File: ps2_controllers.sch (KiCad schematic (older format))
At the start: 11 parts

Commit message: Passing ERC
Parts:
- gave numbers to parts that had none: 11
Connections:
- wire segments 45 -> 49
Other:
- moved on the sheet: D8, D9, P3, P4, R25, R26, R27, R28, R29, R30, SW1

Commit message: Starting on netlist
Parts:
- R25: footprint (none) -> Resistors_SMD:R_0603
- R26, R27, R30: footprint Resistors_SMD:R_0805_HandSoldering -> Resistors_SMD:R_0603
- R28, R29: footprint Resistors_SMD:R_0805_HandSoldering -> Resistors_SMD:R_0805
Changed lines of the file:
@@
 LIBS:w_device
 LIBS:pcb_ledtorus_controller-cache
-LIBS:tiva_pcb1-cache
 EELAYER 26 0
 EELAYER END
@@
 F 0 "R28" V 4130 1800 50  0000 C CNN
 F 1 "1k" V 4050 1800 50  0000 C CNN
-F 2 "Resistors_SMD:R_0805_HandSoldering" V 3980 1800 30  0001 C CNN
+F 2 "Resistors_SMD:R_0805" V 3980 1800 30  0001 C CNN
 F 3 "" H 4050 1800 30  0000 C CNN
 	1    4050 1800
@@
 F 0 "R29" V 5030 1800 50  0000 C CNN
 F 1 "1k" V 4950 1800 50  0000 C CNN
-F 2 "Resistors_SMD:R_0805_HandSoldering" V 4880 1800 30  0001 C CNN
+F 2 "Resistors_SMD:R_0805" V 4880 1800 30  0001 C CNN
 F 3 "" H 4950 1800 30  0000 C CNN
 	1    4950 1800
@@
 F 0 "R26" V 2130 1750 50  0000 C CNN
 F 1 "4k7" V 2050 1750 50  0000 C CNN
-F 2 "Resistors_SMD:R_0805_HandSoldering" V 1980 1750 30  0001 C CNN
+F 2 "Resistors_SMD:R_0603" V 1980 1750 30  0001 C CNN
 F 3 "" H 2050 1750 30  0000 C CNN
 	1    2050 1750
@@
 F 0 "R30" V 2130 3650 50  0000 C CNN
 F 1 "4k7" V 2050 3650 50  0000 C CNN
-F 2 "Resistors_SMD:R_0805_HandSoldering" V 1980 3650 30  0001 C CNN
+F 2 "Resistors_SMD:R_0603" V 1980 3650 30  0001 C CNN
 F 3 "" H 2050 3650 30  0000 C CNN
 	1    2050 3650
@@
 F 0 "R27" V 2780 1750 50  0000 C CNN
 F 1 "4k7" V 2700 1750 50  0000 C CNN
-F 2 "Resistors_SMD:R_0805_HandSoldering" V 2630 1750 30  0001 C CNN
+F 2 "Resistors_SMD:R_0603" V 2630 1750 30  0001 C CNN
 F 3 "" H 2700 1750 30  0000 C CNN
 	1    2700 1750
@@
 F 0 "R25" V 1750 1500 50  0000 C CNN
 F 1 "4k7" V 1850 1500 40  0000 C CNN
-F 2 "" H 1850 1500 50  0001 C CNN
+F 2 "Resistors_SMD:R_0603" H 1850 1500 50  0001 C CNN
 F 3 "" H 1850 1500 50  0001 C CNN
 	1    1850 1500

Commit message: Work on layout
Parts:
- removed D8, D9: LED, LEDs:LED_0805, symbol LED
- removed R28, R29: 1k, Resistors_SMD:R_0805, symbol R
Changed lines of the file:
@@
 	1    0    0    -1
-$EndComp
-$Comp
-L LED D8
-U 1 1 5C262DAB
-P 4050 1550
-F 0 "D8" H 4050 1650 50  0000 C CNN
-F 1 "LED" H 4050 1450 50  0000 C CNN
-F 2 "LEDs:LED_0805" H 4050 1550 60  0001 C CNN
-F 3 "" H 4050 1550 60  0000 C CNN
-	1    4050 1550
-	-1   0    0    -1
-$EndComp
-$Comp
-L LED D9
-U 1 1 5C262DAC
-P 4950 1550
-F 0 "D9" H 4950 1650 50  0000 C CNN
-F 1 "LED" H 4950 1450 50  0000 C CNN
-F 2 "LEDs:LED_0805" H 4950 1550 60  0001 C CNN
-F 3 "" H 4950 1550 60  0000 C CNN
-	1    4950 1550
-	-1   0    0    -1
 $EndComp
 Text Notes 1000 1325 0    120  ~ 24
@@
 Text Notes 1000 3350 0    120  ~ 24
 DualShock2, 2
-$Comp
-L R R28
-U 1 1 5C262DAD
-P 4050 1800
-F 0 "R28" V 4130 1800 50  0000 C CNN
-F 1 "1k" V 4050 1800 50  0000 C CNN
-F 2 "Resistors_SMD:R_0805" V 3980 1800 30  0001 C CNN
-F 3 "" H 4050 1800 30  0000 C CNN
-	1    4050 1800
-	0    1    1    0
-$EndComp
-$Comp
-L R R29
-U 1 1 5C262DAE
-P 4950 1800
-F 0 "R29" V 5030 1800 50  0000 C CNN
-F 1 "1k" V 4950 1800 50  0000 C CNN
-F 2 "Resistors_SMD:R_0805" V 4880 1800 30  0001 C CNN
-F 3 "" H 4950 1800 30  0000 C CNN
-	1    4950 1800
-	0    1    1    0
-$EndComp
 $Comp
 L R R26
@@
 	-1   0    0    1
 $EndComp
-Text Label 4225 1550 0    60   ~ 0
-gpio1
-Text Label 5125 1550 0    60   ~ 0
-gpio2
 Text Label 5775 1950 0    60   ~ 0
 gpio1
@@
 	1    0    0    -1
 $EndComp
-$Comp
-L +3V3 #PWR031
-U 1 1 5C262DB5
-P 5375 1850
-F 0 "#PWR031" H 5375 1700 50  0001 C CNN
-F 1 "+3V3" H 5393 2023 50  0000 C CNN
-F 2 "" H 5375 1850 50  0000 C CNN
-F 3 "" H 5375 1850 50  0000 C CNN
-	1    5375 1850
-	1    0    0    -1
-$EndComp
 Wire Wire Line
 	1500 1600 1700 1600
@@
 Wire Wire Line
 	1600 4000 1600 4475
-Wire Wire Line
-	3900 1550 3900 1800
-Wire Wire Line
-	4800 1550 4800 1800
-Wire Wire Line
-	4200 1800 4300 1800
-Wire Wire Line
-	4300 1800 4300 1950
-Wire Wire Line
-	5100 1800 5175 1800
-Wire Wire Line
-	5175 1800 5175 1950
-Wire Wire Line
-	4200 1550 4500 1550
-Wire Wire Line
-	5100 1550 6050 1550
 Wire Wire Line
 	5750 1950 6050 1950
@@
 	6650 1750 7000 1750
 Connection ~ 7000 1750
-Wire Wire Line
-	4300 1950 5375 1950
-Wire Wire Line
-	5375 1950 5375 1850
-Connection ~ 5175 1950
 Text GLabel 1600 1800 2    45   Input ~ 0
 ps2_clk
@@
 Connection ~ 5600 1550
 Wire Wire Line
-	4500 1550 4500 2050
-Wire Wire Line
-	4500 2050 5750 2050
-Wire Wire Line
 	5750 2050 5750 1950
 Text GLabel 5600 1950 1    45   Output ~ 0
@@
 	5600 1950 5600 2050
 Connection ~ 5600 2050
+Wire Wire Line
+	5600 1550 6050 1550
+Wire Wire Line
+	5600 2050 5750 2050
 $EndSCHEMATC

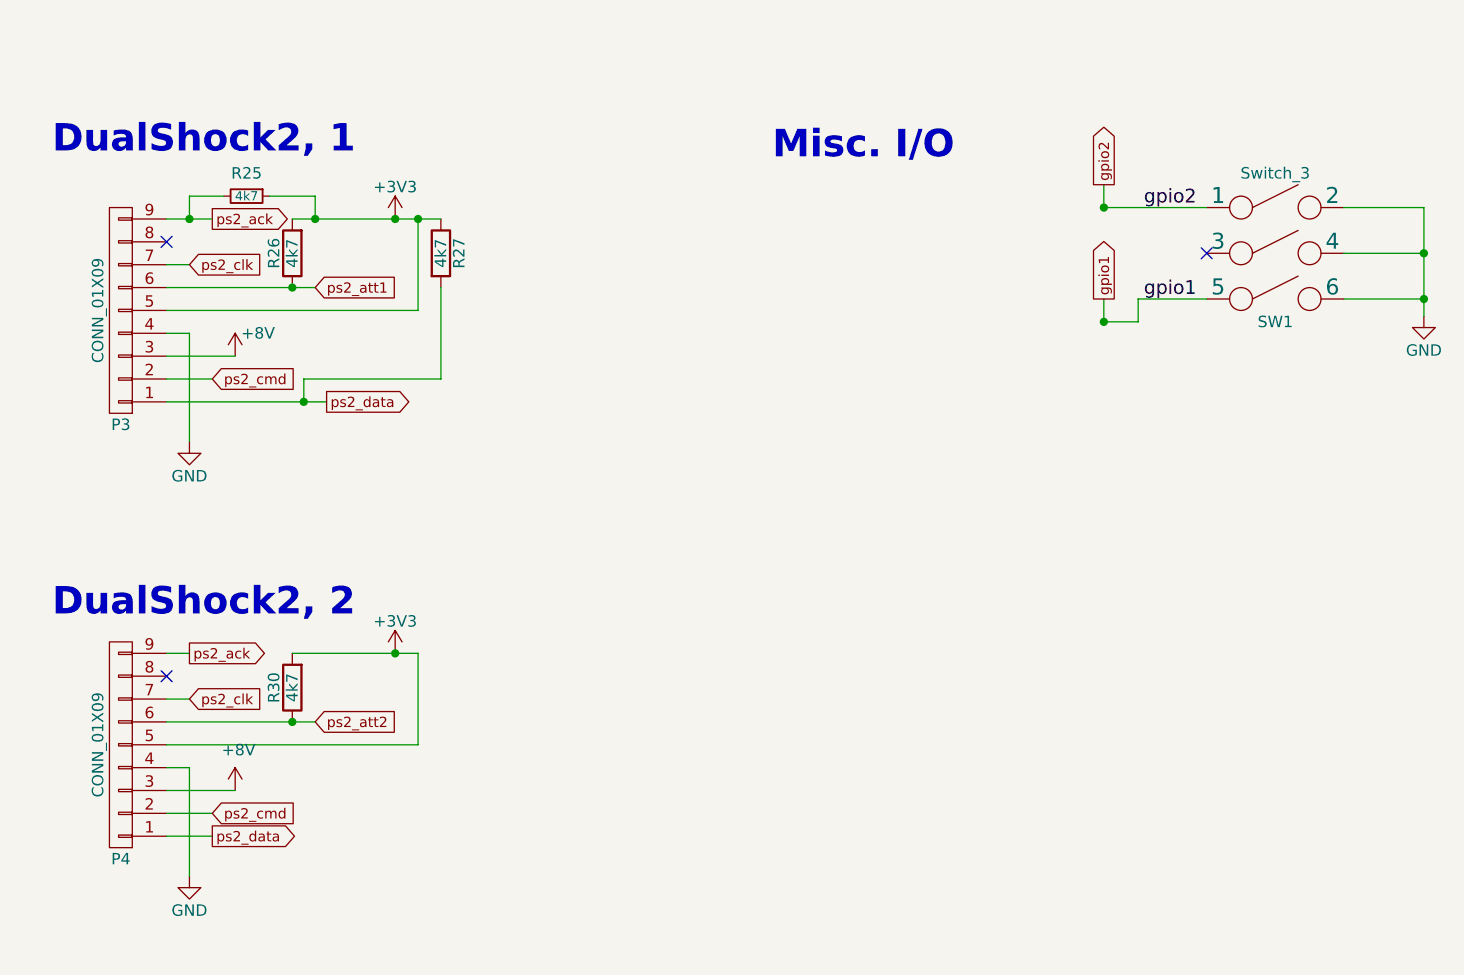
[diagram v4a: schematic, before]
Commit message: Completing cleanups and ToDos:
 - L6234 thermal vias done
 - Gerbers checked
 - Misc. io and stuff tweaks
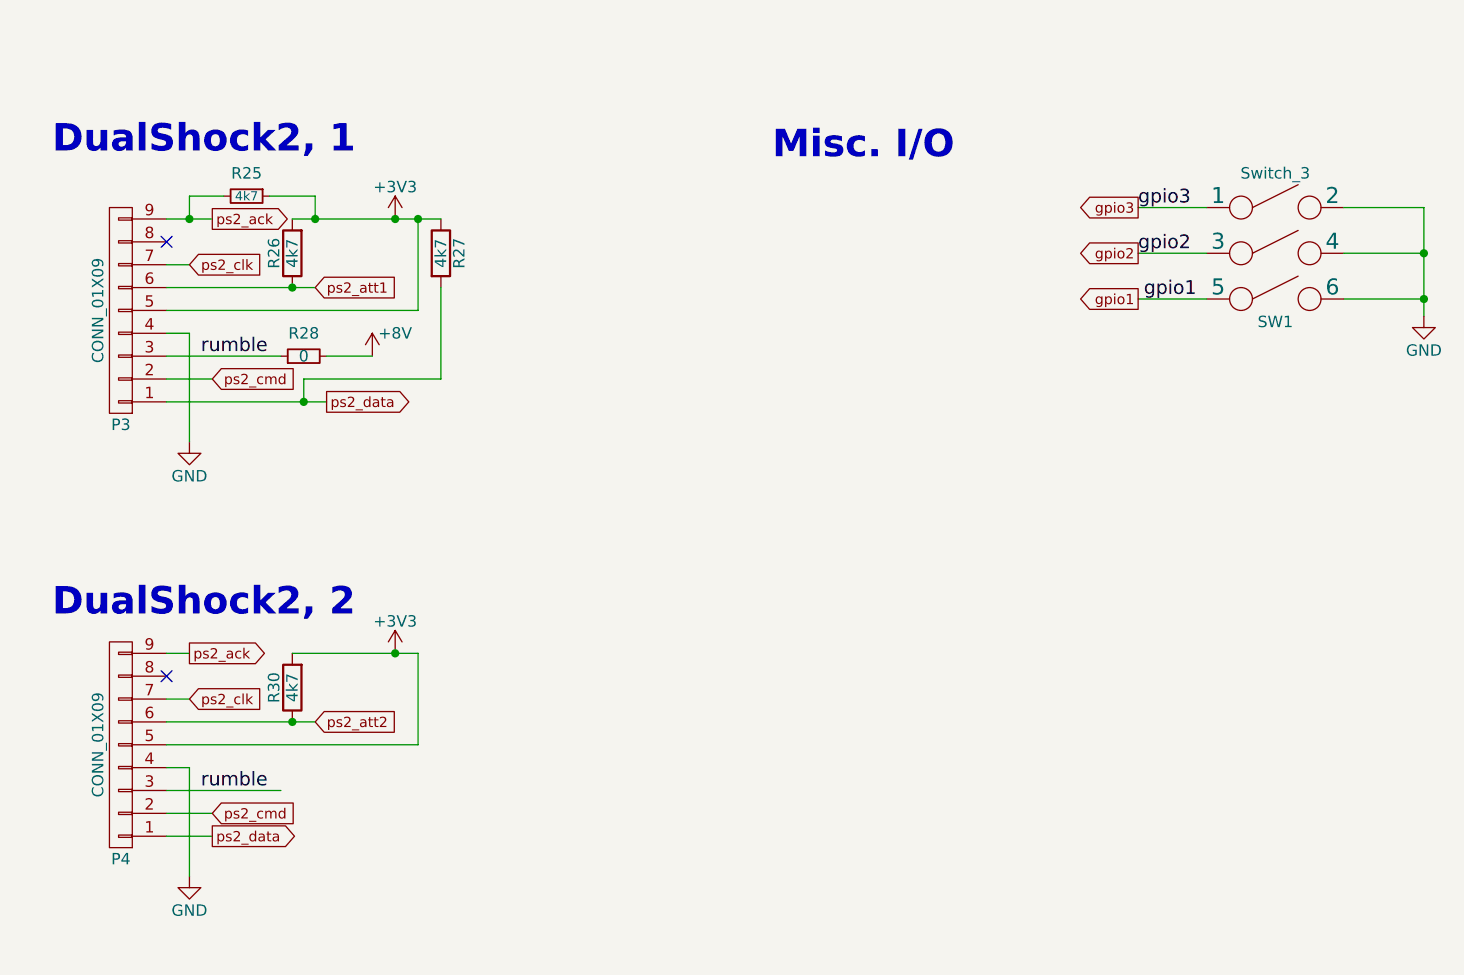
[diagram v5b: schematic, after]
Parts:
- added R28: 0, Resistors_SMD:R_0805, symbol R_Small
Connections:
- net +8V: now also R28.2; no longer P3.3 (P3), P4.3 (P3)
- net gpio2: now also SW1.3; no longer SW1.1
- new net gpio3: SW1.1
- new net rumble: P3.3 (P3), P4.3 (P3), R28.1
- no-connect marks 3 -> 2
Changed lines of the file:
@@
 Text Label 5775 1950 0    60   ~ 0
 gpio1
-Text Label 5775 1550 0    60   ~ 0
+Text Label 5750 1750 0    60   ~ 0
 gpio2
 $Comp
@@
 	1    0    0    -1
 $EndComp
-NoConn ~ 6050 1750
 $Comp
 L R R27
@@
 	1500 2100 1600 2100
 Wire Wire Line
-	1500 2200 1800 2200
+	1500 2200 2000 2200
 Wire Wire Line
 	1500 2300 1700 2300
@@
 	1500 3800 2150 3800
 Wire Wire Line
-	1500 4100 1800 4100
+	1500 4100 2000 4100
 Wire Wire Line
 	1600 2100 1600 2575
@@
 L +8V #PWR033
 U 1 1 5C2803CB
-P 1800 2200
-F 0 "#PWR033" H 1800 2050 50  0001 C CNN
-F 1 "+8V" H 1900 2300 50  0000 C CNN
-F 2 "" H 1800 2200 50  0001 C CNN
-F 3 "" H 1800 2200 50  0001 C CNN
-	1    1800 2200
+P 2400 2200
+F 0 "#PWR033" H 2400 2050 50  0001 C CNN
+F 1 "+8V" H 2500 2300 50  0000 C CNN
+F 2 "" H 2400 2200 50  0001 C CNN
+F 3 "" H 2400 2200 50  0001 C CNN
+	1    2400 2200
 	1    0    0    -1
 $EndComp
 Connection ~ 2100 2400
 Wire Wire Line
-	2600 2000 2600 1600
+	2600 1600 2600 2000
 Wire Wire Line
 	2050 1600 2700 1600
@@
 	1500 3900 2600 3900
 Wire Wire Line
-	2600 3900 2600 3500
+	2600 3500 2600 3900
 Wire Wire Line
-	2600 3500 2050 3500
+	2050 3500 2600 3500
 Connection ~ 2500 3500
 Text GLabel 2150 3800 2    45   Input ~ 0
 ps2_att2
 Connection ~ 2050 3800
-$Comp
-L +8V #PWR036
-U 1 1 5C281018
-P 1800 4100
-F 0 "#PWR036" H 1800 3950 50  0001 C CNN
-F 1 "+8V" H 1815 4277 50  0000 C CNN
-F 2 "" H 1800 4100 50  0001 C CNN
-F 3 "" H 1800 4100 50  0001 C CNN
-	1    1800 4100
-	1    0    0    -1
-$EndComp
 Text GLabel 1700 4300 2    45   Output ~ 0
 ps2_data
@@
 	2150 1500 2150 1600
 Connection ~ 2150 1600
-Text GLabel 5600 1450 1    45   Output ~ 0
-gpio2
-Wire Wire Line
-	5600 1550 5600 1450
-Connection ~ 5600 1550
-Wire Wire Line
-	5750 2050 5750 1950
-Text GLabel 5600 1950 1    45   Output ~ 0
+Text GLabel 5750 1550 0    45   Output ~ 0
+gpio3
+Text GLabel 5750 1950 0    45   Output ~ 0
 gpio1
 Wire Wire Line
-	5600 1950 5600 2050
-Connection ~ 5600 2050
+	5750 1550 6050 1550
+$Comp
+L R_Small R28
+U 1 1 5C7E18F5
+P 2100 2200
+F 0 "R28" V 2200 2200 50  0000 C CNN
+F 1 "0" V 2100 2200 50  0000 C CNN
+F 2 "Resistors_SMD:R_0805" H 2100 2200 50  0001 C CNN
+F 3 "" H 2100 2200 50  0001 C CNN
+	1    2100 2200
+	0    -1   -1   0
+$EndComp
 Wire Wire Line
-	5600 1550 6050 1550
+	2200 2200 2400 2200
+Text Label 1650 4100 0    60   ~ 0
+rumble
+Text Label 1650 2200 0    60   ~ 0
+rumble
 Wire Wire Line
-	5600 2050 5750 2050
+	6050 1750 5750 1750
+Text Label 5750 1550 0    60   ~ 0
+gpio3
+Text GLabel 5750 1750 0    45   Output ~ 0
+gpio2
 $EndSCHEMATC

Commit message: Submitted rev1 for production @ SeeedStudio
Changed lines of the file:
@@
 Connection ~ 2100 2400
 Wire Wire Line
-	2600 1600 2600 2000
+	2600 2000 2600 1600
 Wire Wire Line
 	2050 1600 2700 1600
@@
 	1500 3900 2600 3900
 Wire Wire Line
-	2600 3500 2600 3900
+	2600 3900 2600 3500
 Wire Wire Line
-	2050 3500 2600 3500
+	2600 3500 2050 3500
 Connection ~ 2500 3500
 Text GLabel 2150 3800 2    45   Input ~ 0
